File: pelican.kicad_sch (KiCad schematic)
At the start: 0 parts

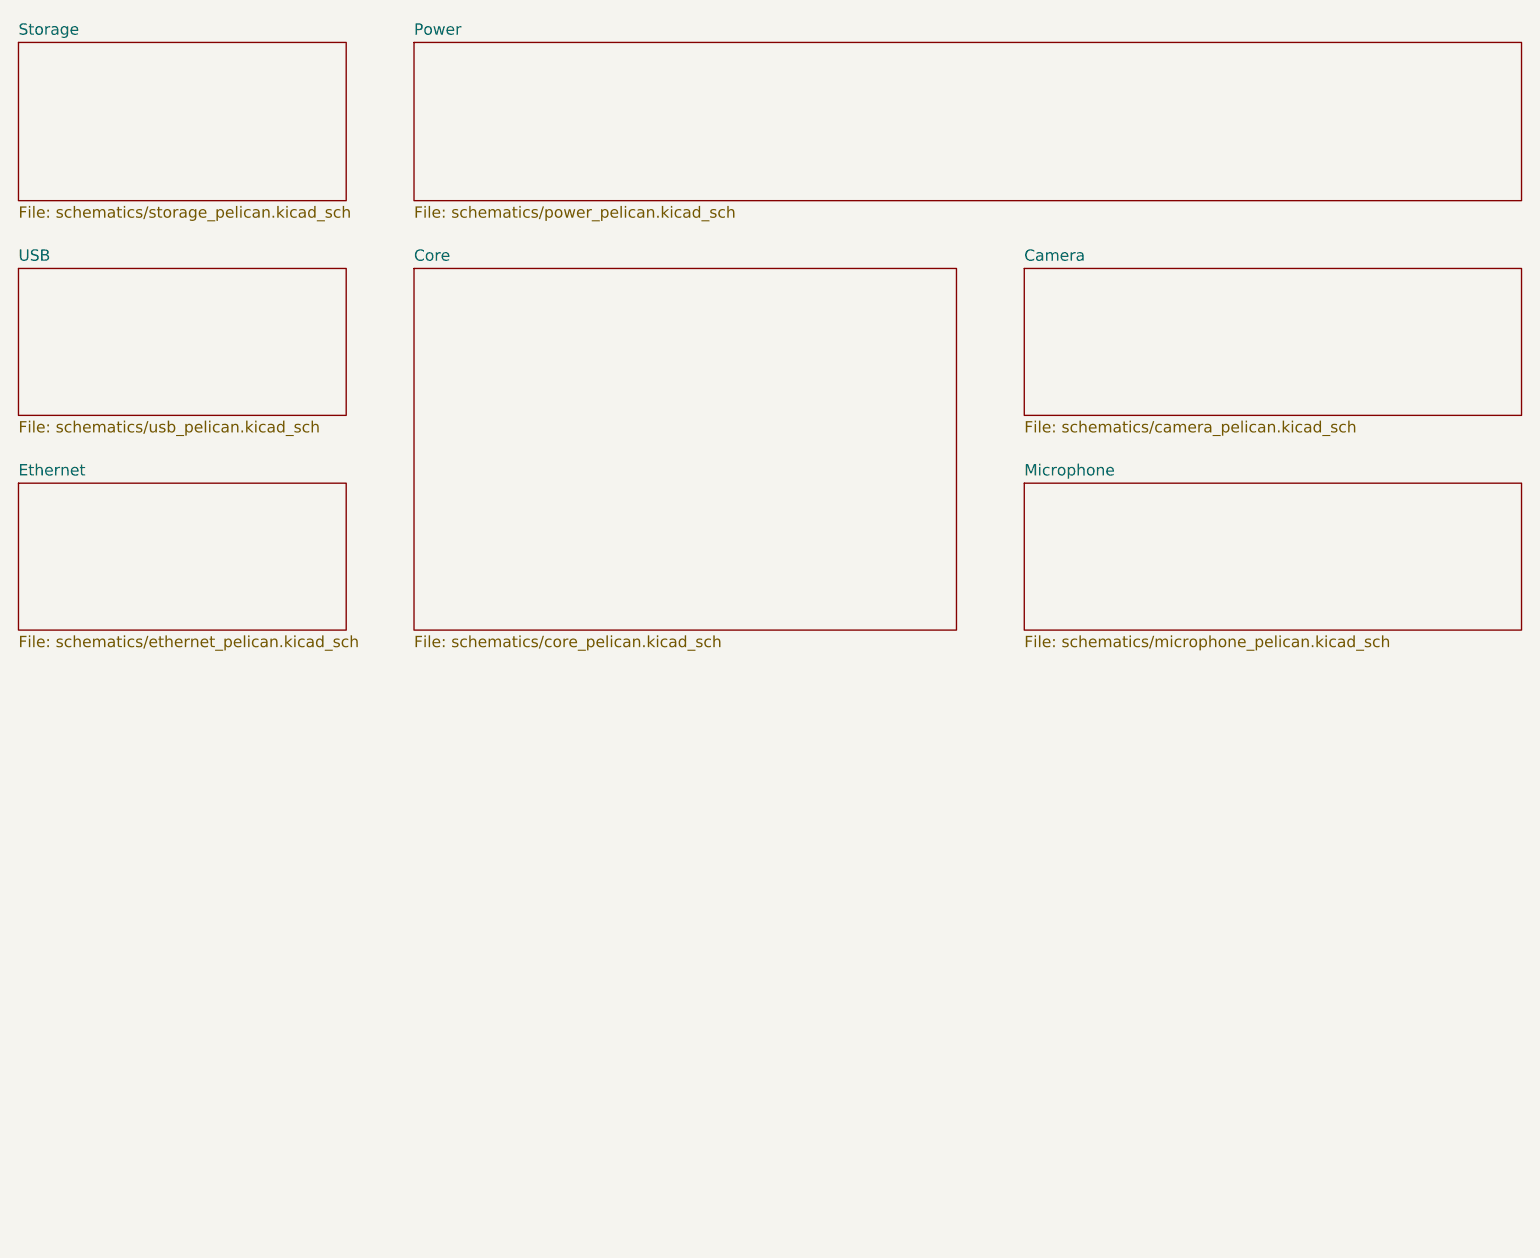
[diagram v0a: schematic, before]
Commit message: updated schematic based on review
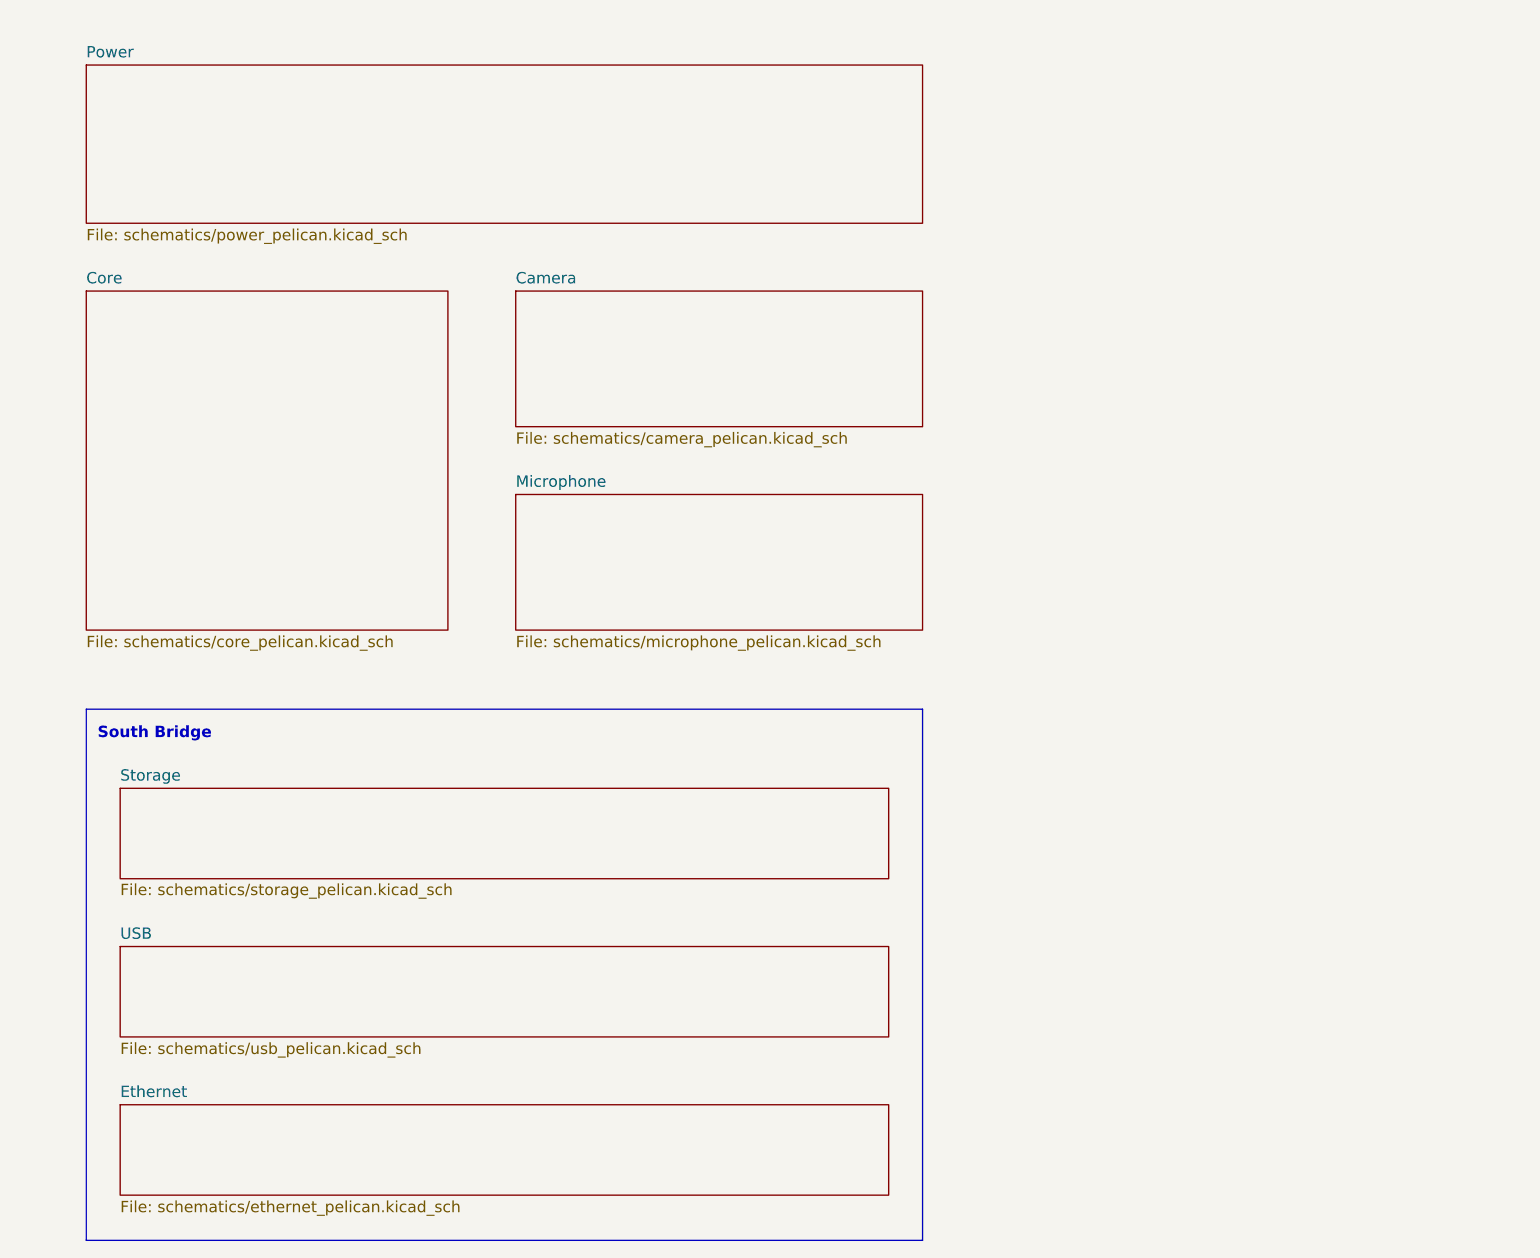
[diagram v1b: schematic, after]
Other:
- note added: "South Bridge"
